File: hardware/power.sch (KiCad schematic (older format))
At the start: 18 parts

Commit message: przeniosiono do folderu hardware
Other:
- note added: "analog & digital voltage split\n"
- note removed: "voltage analog & digital voltage split\n"
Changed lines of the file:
@@
 U 1 1 5D6AB170
 P 7400 3850
+AR Path="/5CDEAB6D/5D6AB170" Ref="FB?"  Part="1"
+AR Path="/5CDEEC5A/5D6AB170" Ref="FB?"  Part="1"
 F 0 "FB?" H 7500 3896 50  0000 L CNN
 F 1 "Ferrite_Bead_Small" H 7500 3805 50  0000 L CNN
@@
 U 1 1 5D6AB176
 P 7650 3850
+AR Path="/5CDEAB6D/5D6AB176" Ref="#PWR?"  Part="1"
+AR Path="/5CDEEC5A/5D6AB176" Ref="#PWR?"  Part="1"
 F 0 "#PWR?" H 7650 3700 50  0001 C CNN
 F 1 "+3.3V" V 7665 3978 50  0000 L CNN
@@
 	6650 3400 6650 3700
 Text Notes 6650 3350 0    50   ~ 0
-voltage analog & digital voltage split\n
+analog & digital voltage split\n
 $EndSCHEMATC

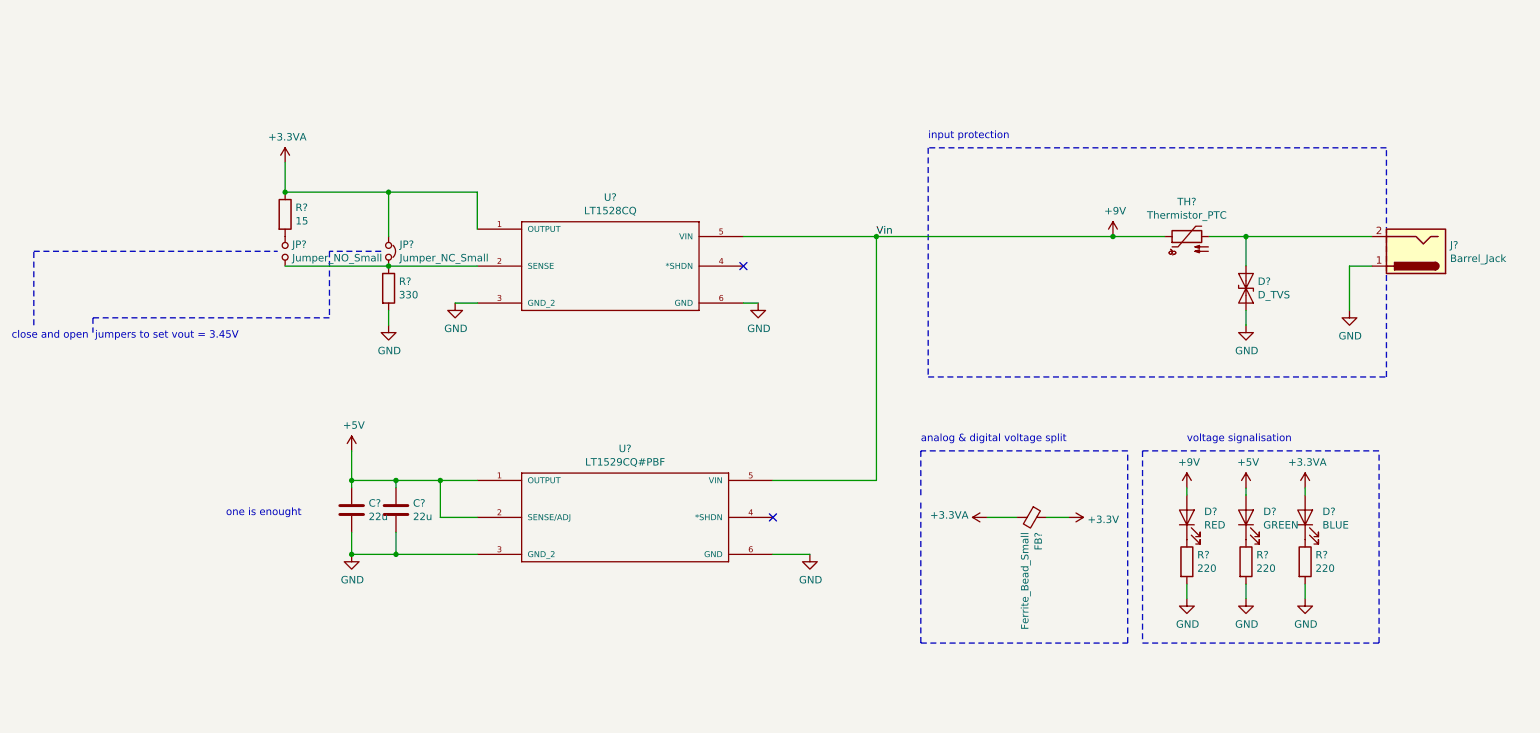
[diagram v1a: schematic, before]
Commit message: DRC przechodzi dorzucone złącze do wyświetlacza na i2c oraz jeden push button
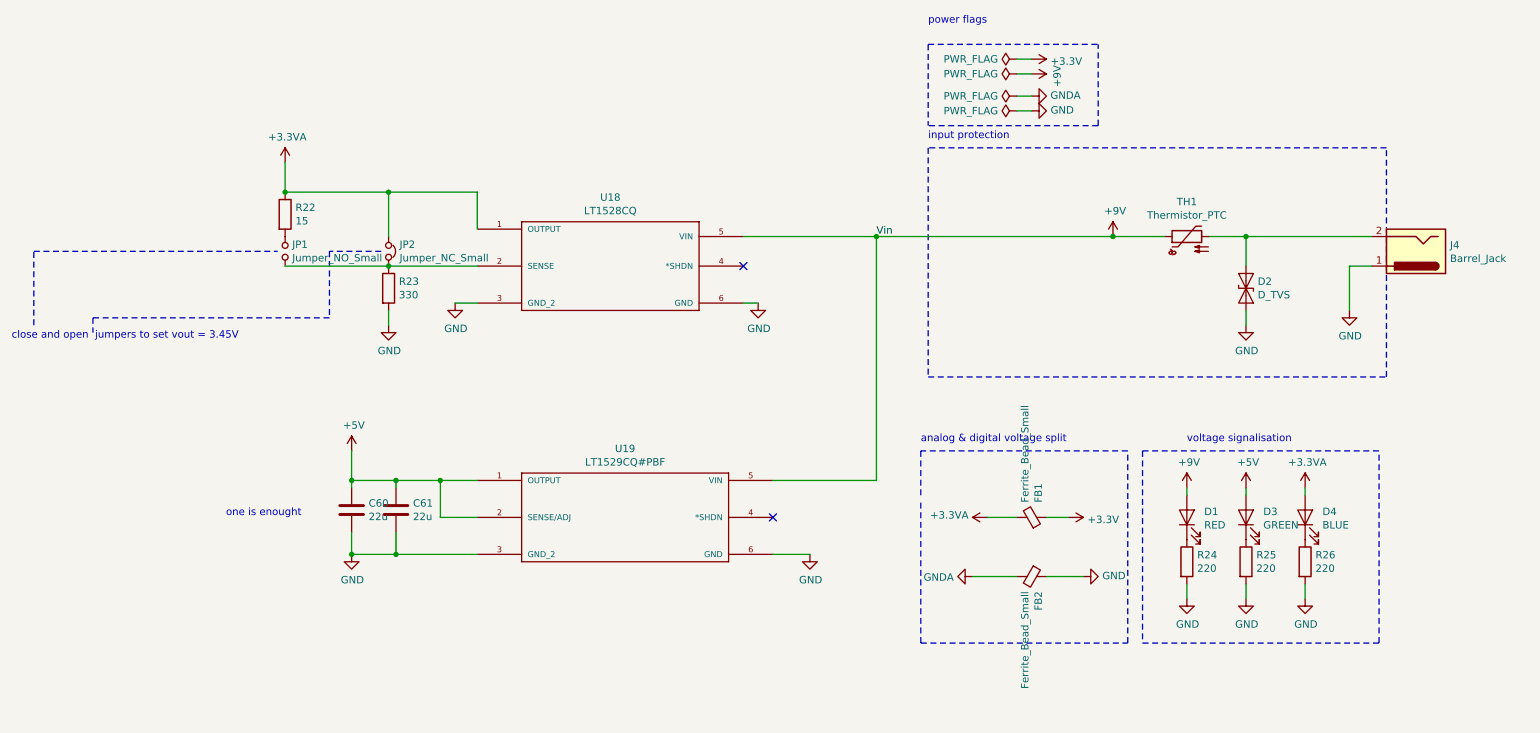
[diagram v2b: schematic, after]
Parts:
- added FB2: Ferrite_Bead_Small, symbol Device:Ferrite_Bead_Small
- gave numbers to parts that had none: 18
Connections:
- net GND: now also FB2.1
- new net GNDA: FB2.2
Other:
- note added: "power flags\n\n"

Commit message: przypisano footprinty
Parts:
- C60, C61: footprint (none) -> Capacitor_SMD:C_0805_2012Metric_Pad1.15x1.40mm_HandSolder
- D1, D3, D4: footprint (none) -> LED_SMD:LED_0805_2012Metric
- D2: footprint (none) -> Diode_SMD:D_SOD-323
- FB1, FB2: footprint (none) -> Inductor_SMD:L_0805_2012Metric_Pad1.15x1.40mm_HandSolder
- J4: footprint (none) -> Connector_BarrelJack:BarrelJack_Horizontal
- JP1: footprint (none) -> Jumper:SolderJumper-2_P1.3mm_Open_TrianglePad1.0x1.5mm
- JP2: footprint (none) -> Jumper:SolderJumper-2_P1.3mm_Bridged_Pad1.0x1.5mm
- R22, R23, R24, R25, R26: footprint (none) -> Resistor_SMD:R_0603_1608Metric_Pad1.05x0.95mm_HandSolder
- TH1: footprint (none) -> Fuse:Fuse_1812_4532Metric
- U18, U19: footprint DDPAK-5_Q -> symbols:DDPAK-5_Q
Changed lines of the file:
@@
 $Descr A4 11693 8268
 encoding utf-8
-Sheet 5 4
+Sheet 4 4
 Title ""
 Date ""
@@
 F 0 "U18" H 4550 2415 50  0000 C CNN
 F 1 "LT1528CQ" H 4550 2324 50  0000 C CNN
-F 2 "DDPAK-5_Q" H 3650 2050 50  0001 L BNN
+F 2 "symbols:DDPAK-5_Q" H 3650 2050 50  0001 L BNN
 F 3 "" H 3650 2050 50  0001 L BNN
 F 4 "None" H 3650 2050 50  0001 L BNN "Pole4"
@@
 F 0 "U19" H 4650 4115 50  0000 C CNN
 F 1 "LT1529CQ#PBF" H 4650 4024 50  0000 C CNN
-F 2 "DDPAK-5_Q" H 3650 3750 50  0001 L BNN
+F 2 "symbols:DDPAK-5_Q" H 3650 3750 50  0001 L BNN
 F 3 "" H 3650 3750 50  0001 L BNN
 F 4 "TO-263 Linear Technology" H 3650 3750 50  0001 L BNN "Pole4"
@@
 F 0 "R23" H 3120 2346 50  0000 L CNN
 F 1 "330" H 3120 2255 50  0000 L CNN
-F 2 "" V 2980 2300 50  0001 C CNN
+F 2 "Resistor_SMD:R_0603_1608Metric_Pad1.05x0.95mm_HandSolder" V 2980 2300 50  0001 C CNN
 F 3 "~" H 3050 2300 50  0001 C CNN
 	1    3050 2300
@@
 F 0 "R22" H 2420 1846 50  0000 L CNN
 F 1 "15" H 2420 1755 50  0000 L CNN
-F 2 "" V 2280 1800 50  0001 C CNN
+F 2 "Resistor_SMD:R_0603_1608Metric_Pad1.05x0.95mm_HandSolder" V 2280 1800 50  0001 C CNN
 F 3 "~" H 2350 1800 50  0001 C CNN
 	1    2350 1800
@@
 F 0 "JP2" V 3004 2124 50  0000 L CNN
 F 1 "Jumper_NC_Small" V 3095 2124 50  0000 L CNN
-F 2 "" H 3050 2050 50  0001 C CNN
+F 2 "Jumper:SolderJumper-2_P1.3mm_Bridged_Pad1.0x1.5mm" H 3050 2050 50  0001 C CNN
 F 3 "~" H 3050 2050 50  0001 C CNN
 	1    3050 2050
@@
 F 0 "JP1" V 2396 2002 50  0000 R CNN
 F 1 "Jumper_NO_Small" V 2305 2002 50  0000 R CNN
-F 2 "" H 2350 2050 50  0001 C CNN
+F 2 "Jumper:SolderJumper-2_P1.3mm_Open_TrianglePad1.0x1.5mm" H 2350 2050 50  0001 C CNN
 F 3 "~" H 2350 2050 50  0001 C CNN
 	1    2350 2050
@@
 F 0 "C60" H 2915 3846 50  0000 L CNN
 F 1 "22u" H 2915 3755 50  0000 L CNN
-F 2 "" H 2838 3650 50  0001 C CNN
+F 2 "Capacitor_SMD:C_0805_2012Metric_Pad1.15x1.40mm_HandSolder" H 2838 3650 50  0001 C CNN
 F 3 "~" H 2800 3800 50  0001 C CNN
 	1    2800 3800
@@
 F 0 "C61" H 3215 3846 50  0000 L CNN
 F 1 "22u" H 3215 3755 50  0000 L CNN
-F 2 "" H 3138 3650 50  0001 C CNN
+F 2 "Capacitor_SMD:C_0805_2012Metric_Pad1.15x1.40mm_HandSolder" H 3138 3650 50  0001 C CNN
 F 3 "~" H 3100 3800 50  0001 C CNN
 	1    3100 3800
@@
 F 0 "J4" H 9770 2008 50  0000 R CNN
 F 1 "Barrel_Jack" H 9770 2099 50  0000 R CNN
-F 2 "" H 10050 2010 50  0001 C CNN
+F 2 "Connector_BarrelJack:BarrelJack_Horizontal" H 10050 2010 50  0001 C CNN
 F 3 "~" H 10050 2010 50  0001 C CNN
 	1    10000 2050
@@
 F 0 "D4" V 9289 3733 50  0000 R CNN
 F 1 "BLUE" V 9198 3733 50  0000 R CNN
-F 2 "" H 9250 3850 50  0001 C CNN
+F 2 "LED_SMD:LED_0805_2012Metric" H 9250 3850 50  0001 C CNN
 F 3 "~" H 9250 3850 50  0001 C CNN
 	1    9250 3850
@@
 F 0 "R26" H 9320 4196 50  0000 L CNN
 F 1 "220" H 9320 4105 50  0000 L CNN
-F 2 "" V 9180 4150 50  0001 C CNN
+F 2 "Resistor_SMD:R_0603_1608Metric_Pad1.05x0.95mm_HandSolder" V 9180 4150 50  0001 C CNN
 F 3 "~" H 9250 4150 50  0001 C CNN
 	1    9250 4150
@@
 F 0 "D3" V 8889 3733 50  0000 R CNN
 F 1 "GREEN" V 8798 3733 50  0000 R CNN
-F 2 "" H 8850 3850 50  0001 C CNN
+F 2 "LED_SMD:LED_0805_2012Metric" H 8850 3850 50  0001 C CNN
 F 3 "~" H 8850 3850 50  0001 C CNN
 	1    8850 3850
@@
 F 0 "R25" H 8920 4196 50  0000 L CNN
 F 1 "220" H 8920 4105 50  0000 L CNN
-F 2 "" V 8780 4150 50  0001 C CNN
+F 2 "Resistor_SMD:R_0603_1608Metric_Pad1.05x0.95mm_HandSolder" V 8780 4150 50  0001 C CNN
 F 3 "~" H 8850 4150 50  0001 C CNN
 	1    8850 4150
@@
 F 0 "D1" V 8489 3733 50  0000 R CNN
 F 1 "RED" V 8398 3733 50  0000 R CNN
-F 2 "" H 8450 3850 50  0001 C CNN
+F 2 "LED_SMD:LED_0805_2012Metric" H 8450 3850 50  0001 C CNN
 F 3 "~" H 8450 3850 50  0001 C CNN
 	1    8450 3850
@@
 F 0 "R24" H 8520 4196 50  0000 L CNN
 F 1 "220" H 8520 4105 50  0000 L CNN
-F 2 "" V 8380 4150 50  0001 C CNN
+F 2 "Resistor_SMD:R_0603_1608Metric_Pad1.05x0.95mm_HandSolder" V 8380 4150 50  0001 C CNN
 F 3 "~" H 8450 4150 50  0001 C CNN
 	1    8450 4150
@@
 F 0 "TH1" V 8685 1950 50  0000 C CNN
 F 1 "Thermistor_PTC" V 8594 1950 50  0000 C CNN
-F 2 "" H 8500 1750 50  0001 L CNN
+F 2 "Fuse:Fuse_1812_4532Metric" H 8500 1750 50  0001 L CNN
 F 3 "~" H 8450 1950 50  0001 C CNN
 	1    8450 1950
@@
 F 0 "D2" V 8804 2379 50  0000 L CNN
 F 1 "D_TVS" V 8895 2379 50  0000 L CNN
-F 2 "" H 8850 2300 50  0001 C CNN
+F 2 "Diode_SMD:D_SOD-323" H 8850 2300 50  0001 C CNN
 F 3 "~" H 8850 2300 50  0001 C CNN
 	1    8850 2300
@@
 F 0 "FB1" H 7500 3896 50  0000 L CNN
 F 1 "Ferrite_Bead_Small" H 7500 3805 50  0000 L CNN
-F 2 "" V 7330 3850 50  0001 C CNN
+F 2 "Inductor_SMD:L_0805_2012Metric_Pad1.15x1.40mm_HandSolder" V 7330 3850 50  0001 C CNN
 F 3 "~" H 7400 3850 50  0001 C CNN
 	1    7400 3850
@@
 F 0 "FB2" H 7500 4296 50  0000 L CNN
 F 1 "Ferrite_Bead_Small" H 7500 4205 50  0000 L CNN
-F 2 "" V 7330 4250 50  0001 C CNN
+F 2 "Inductor_SMD:L_0805_2012Metric_Pad1.15x1.40mm_HandSolder" V 7330 4250 50  0001 C CNN
 F 3 "~" H 7400 4250 50  0001 C CNN
 	1    7400 4250

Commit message: Dodenie pullup do spi i i2c
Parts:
- D2: footprint Diode_SMD:D_SOD-323 -> Diode_SMD:D_SMB
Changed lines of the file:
@@
 F 0 "D2" V 8804 2379 50  0000 L CNN
 F 1 "D_TVS" V 8895 2379 50  0000 L CNN
-F 2 "Diode_SMD:D_SOD-323" H 8850 2300 50  0001 C CNN
+F 2 "Diode_SMD:D_SMB" H 8850 2300 50  0001 C CNN
 F 3 "~" H 8850 2300 50  0001 C CNN
 	1    8850 2300

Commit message: pierwszy układ PCB
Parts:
- added C62, C63: 10u, Capacitor_SMD:C_0805_2012Metric_Pad1.15x1.40mm_HandSolder, symbol Device:C
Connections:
- net +5V: now also U18.5 (VIN), C63.1
- net +9V: now also C62.1; no longer U18.5 (VIN)
- net GND: now also C62.2, C63.2
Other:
- moved on the sheet: C60, C61, JP1, JP2, R22, R23, U18, U19

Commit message: update pinoutu, zmiany footprintów
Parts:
- removed JP1: Jumper_NO_Small, Jumper:SolderJumper-2_P1.3mm_Open_TrianglePad1.0x1.5mm, symbol Device:Jumper_NO_Small
- R22: value 15 -> N.C
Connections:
- net +9V: now also D2.1 (A1)
- net at JP2.2, R23.1, U18.2 (SENSE): now also R22.2
- net at J4.2, TH1.2: no longer D2.1 (A1)
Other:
- note added: "open jumper to set vout = 3.45V\nset R to 15"
- note removed: "close and open jumpers to set vout = 3.45V\n"
- moved on the sheet: D2
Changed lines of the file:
@@
 P 2650 4050
 F 0 "R22" H 2720 4096 50  0000 L CNN
-F 1 "15" H 2720 4005 50  0000 L CNN
+F 1 "N.C" H 2720 4005 50  0000 L CNN
 F 2 "Resistor_SMD:R_0603_1608Metric_Pad1.05x0.95mm_HandSolder" V 2580 4050 50  0001 C CNN
 F 3 "~" H 2650 4050 50  0001 C CNN
@@
 Wire Wire Line
 	5850 4650 5750 4650
-$Comp
-L Device:Jumper_NO_Small JP1
-U 1 1 5CEC3FA4
-P 2650 4300
-F 0 "JP1" V 2696 4252 50  0000 R CNN
-F 1 "Jumper_NO_Small" V 2605 4252 50  0000 R CNN
-F 2 "Jumper:SolderJumper-2_P1.3mm_Open_TrianglePad1.0x1.5mm" H 2650 4300 50  0001 C CNN
-F 3 "~" H 2650 4300 50  0001 C CNN
-	1    2650 4300
-	0    -1   -1   0
-$EndComp
 Wire Wire Line
 	2650 4400 3350 4400
@@
 	2650 3900 3350 3900
 Text Notes 800  4900 0    50   ~ 0
-close and open  jumpers to set vout = 3.45V\n
+open  jumper to set vout = 3.45V\nset R to 15
 Connection ~ 2650 3900
 NoConn ~ 5600 2200
@@
 Wire Wire Line
 	2750 2450 3050 2450
-Wire Notes Line
-	950  4800 950  4300
-Wire Notes Line
-	950  4300 2600 4300
 Wire Notes Line
 	3300 4300 2950 4300
@@
 $EndComp
 Wire Wire Line
-	8300 1950 7950 1950
+	8300 1950 8150 1950
 $Comp
 L Device:D_TVS D2
 U 1 1 5D3648D0
-P 8850 2300
-F 0 "D2" V 8804 2379 50  0000 L CNN
-F 1 "D_TVS" V 8895 2379 50  0000 L CNN
-F 2 "Diode_SMD:D_SMB" H 8850 2300 50  0001 C CNN
-F 3 "~" H 8850 2300 50  0001 C CNN
-	1    8850 2300
+P 8150 2300
+F 0 "D2" V 8104 2379 50  0000 L CNN
+F 1 "D_TVS" V 8195 2379 50  0000 L CNN
+F 2 "Diode_SMD:D_SMB" H 8150 2300 50  0001 C CNN
+F 3 "~" H 8150 2300 50  0001 C CNN
+	1    8150 2300
 	0    1    1    0
 $EndComp
 Wire Wire Line
-	8850 1950 8850 2150
-Connection ~ 8850 1950
-Wire Wire Line
-	8850 1950 8600 1950
+	8150 1950 8150 2150
 $Comp
 L power:GND #PWR0128
 U 1 1 5D365DC5
-P 8850 2550
-F 0 "#PWR0128" H 8850 2300 50  0001 C CNN
-F 1 "GND" H 8855 2377 50  0000 C CNN
-F 2 "" H 8850 2550 50  0001 C CNN
-F 3 "" H 8850 2550 50  0001 C CNN
-	1    8850 2550
-	1    0    0    -1
-$EndComp
-Wire Wire Line
-	8850 2450 8850 2550
-Wire Wire Line
-	8850 1950 9700 1950
+P 8150 2550
+F 0 "#PWR0128" H 8150 2300 50  0001 C CNN
+F 1 "GND" H 8155 2377 50  0000 C CNN
+F 2 "" H 8150 2550 50  0001 C CNN
+F 3 "" H 8150 2550 50  0001 C CNN
+	1    8150 2550
+	1    0    0    -1
+$EndComp
+Wire Wire Line
+	8150 2450 8150 2550
 $Comp
 L power:+3.3VA #PWR0116
@@
 	6050 2450 6050 2250
 Connection ~ 5850 2450
+Connection ~ 8150 1950
+Wire Wire Line
+	8150 1950 7950 1950
+Wire Wire Line
+	8600 1950 9700 1950
+Wire Wire Line
+	2650 4200 2650 4400
+Wire Notes Line
+	800  4850 650  4850
+Wire Notes Line
+	650  4050 650  4850
+Wire Notes Line
+	650  4050 2550 4050
 $EndSCHEMATC

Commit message: dodanie zabezpieczen portów i dzialniki napiec na wejsciach adc
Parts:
- renumbered C60 to C62, C61 to C63, C62 to C64, C63 to C65, D1 to D3, D3 to D4, D4 to D5, J4 to J7, JP2 to JP1, R22 to R50, R23 to R51, R24 to R52, R25 to R53, R26 to R54, U19 to U18, U18 to U19

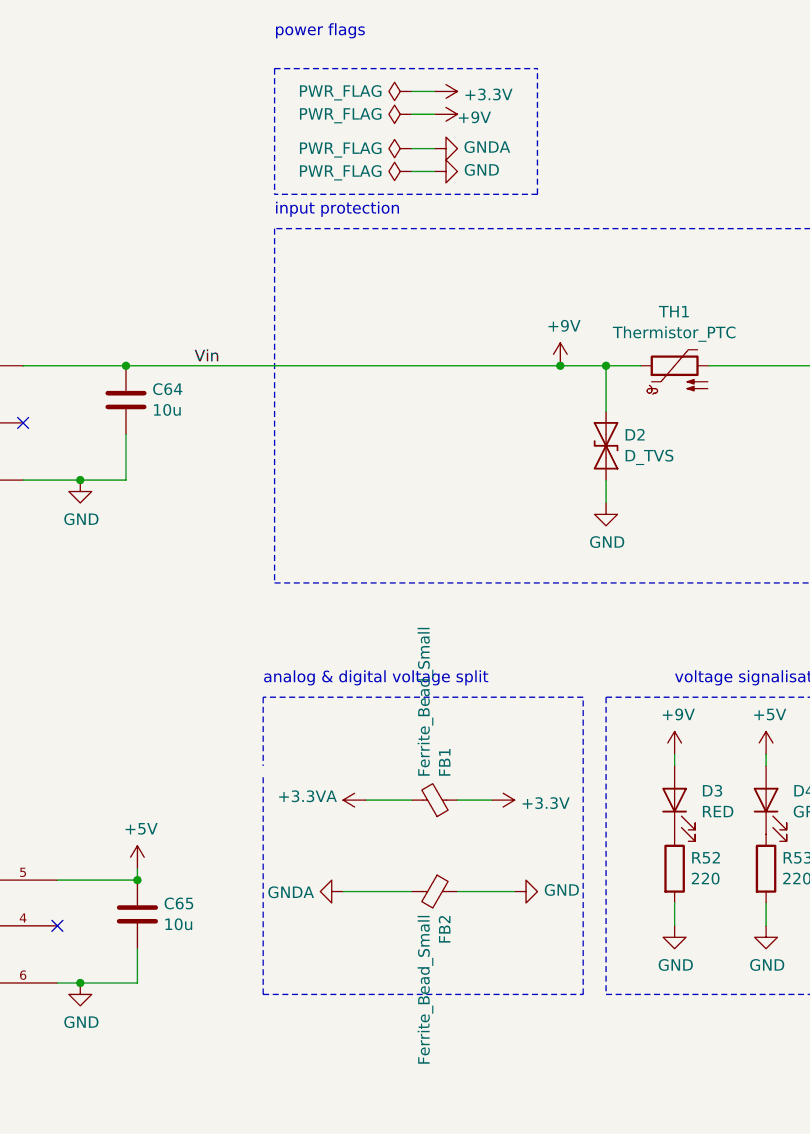
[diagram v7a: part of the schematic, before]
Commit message: layout gotów, do wyeliminowania błedy DRC
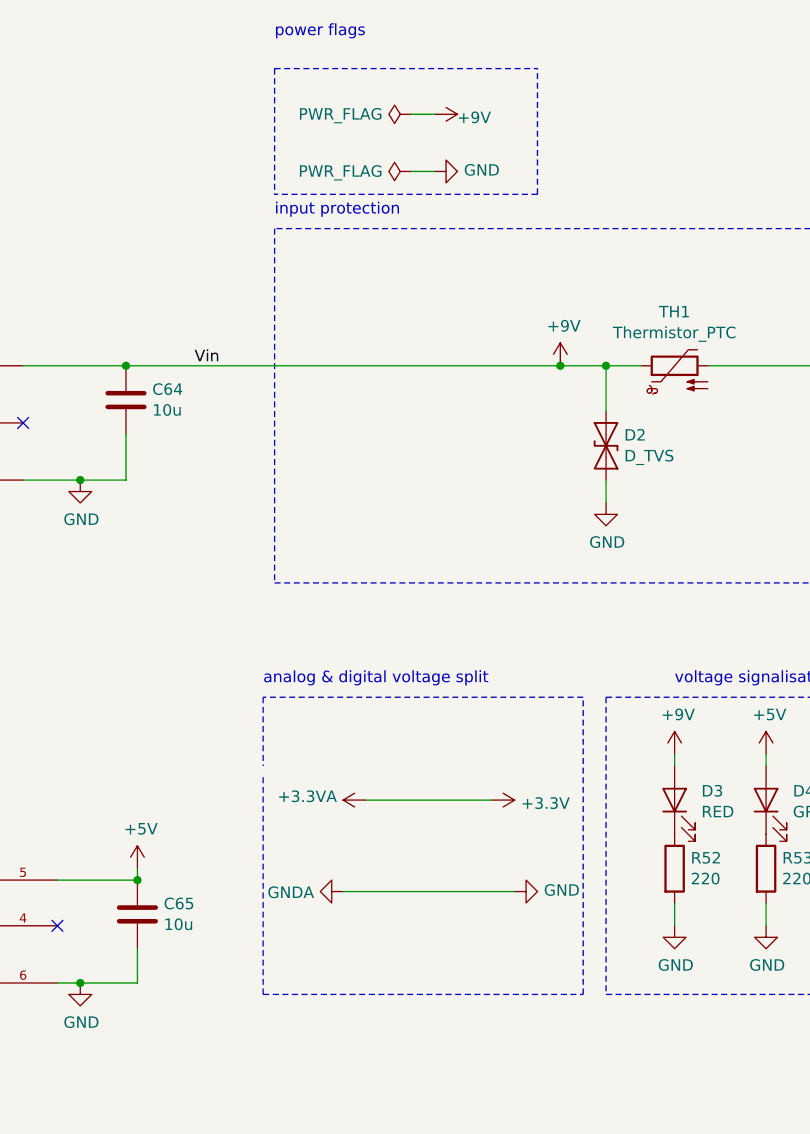
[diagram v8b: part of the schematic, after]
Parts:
- removed FB1, FB2: Ferrite_Bead_Small, Inductor_SMD:L_0805_2012Metric_Pad1.15x1.40mm_HandSolder, symbol Device:Ferrite_Bead_Small
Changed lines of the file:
@@
-$EndComp
-$Comp
-L Device:Ferrite_Bead_Small FB?
-U 1 1 5D6AB170
-P 7400 3850
-AR Path="/5CDEAB6D/5D6AB170" Ref="FB?"  Part="1"
-AR Path="/5CDEEC5A/5D6AB170" Ref="FB1"  Part="1"
-F 0 "FB1" H 7500 3896 50  0000 L CNN
-F 1 "Ferrite_Bead_Small" H 7500 3805 50  0000 L CNN
-F 2 "Inductor_SMD:L_0805_2012Metric_Pad1.15x1.40mm_HandSolder" V 7330 3850 50  0001 C CNN
-F 3 "~" H 7400 3850 50  0001 C CNN
-	1    7400 3850
-	0    1    -1   0
 $EndComp
 $Comp
@@
 	0    1    1    0
 $EndComp
-Wire Wire Line
-	7650 3850 7500 3850
 $Comp
 L power:+3.3VA #PWR0146
@@
 	0    -1   -1   0
 $EndComp
-Wire Wire Line
-	7100 3850 7300 3850
 Wire Notes Line
 	6650 3750 6650 4700
@@
 Text Notes 6650 3350 0    50   ~ 0
 analog & digital voltage split\n
-$Comp
-L power:PWR_FLAG #FLG01
-U 1 1 5D20679D
-P 7300 750
-F 0 "#FLG01" H 7300 825 50  0001 C CNN
-F 1 "PWR_FLAG" V 7300 877 50  0000 L CNN
-F 2 "" H 7300 750 50  0001 C CNN
-F 3 "~" H 7300 750 50  0001 C CNN
-	1    7300 750
-	0    -1   -1   0
-$EndComp
 $Comp
 L power:GNDA #PWR?
@@
 	0    -1   -1   0
 $EndComp
-$Comp
-L Device:Ferrite_Bead_Small FB?
-U 1 1 5D2119F7
-P 7400 4250
-AR Path="/5CDEAB6D/5D2119F7" Ref="FB?"  Part="1"
-AR Path="/5CDEEC5A/5D2119F7" Ref="FB2"  Part="1"
-F 0 "FB2" H 7500 4296 50  0000 L CNN
-F 1 "Ferrite_Bead_Small" H 7500 4205 50  0000 L CNN
-F 2 "Inductor_SMD:L_0805_2012Metric_Pad1.15x1.40mm_HandSolder" V 7330 4250 50  0001 C CNN
-F 3 "~" H 7400 4250 50  0001 C CNN
-	1    7400 4250
-	0    1    1    0
-$EndComp
-Wire Wire Line
-	7750 4250 7500 4250
-Wire Wire Line
-	7300 4250 7000 4250
 Text Notes 6700 600  0    50   ~ 0
 power flags\n\n
@@
 $EndComp
 $Comp
-L power:PWR_FLAG #FLG03
-U 1 1 5D21BB43
-P 7300 1000
-F 0 "#FLG03" H 7300 1075 50  0001 C CNN
-F 1 "PWR_FLAG" V 7300 1127 50  0000 L CNN
-F 2 "" H 7300 1000 50  0001 C CNN
-F 3 "~" H 7300 1000 50  0001 C CNN
-	1    7300 1000
-	0    -1   -1   0
-$EndComp
-$Comp
 L power:GND #PWR?
 U 1 1 5D21C471
@@
 	1    7400 1100
 	0    -1   -1   0
-$EndComp
-$Comp
-L power:GNDA #PWR?
-U 1 1 5D21C8EE
-P 7400 1000
-AR Path="/5CDEAB6D/5D21C8EE" Ref="#PWR?"  Part="1"
-AR Path="/5CDEEC5A/5D21C8EE" Ref="#PWR0149"  Part="1"
-F 0 "#PWR0149" H 7400 750 50  0001 C CNN
-F 1 "GNDA" V 7405 873 50  0000 R CNN
-F 2 "" H 7400 1000 50  0001 C CNN
-F 3 "" H 7400 1000 50  0001 C CNN
-	1    7400 1000
-	0    -1   -1   0
-$EndComp
-$Comp
-L power:+3.3V #PWR?
-U 1 1 5D21CE94
-P 7400 750
-AR Path="/5CDEAB6D/5D21CE94" Ref="#PWR?"  Part="1"
-AR Path="/5CDEEC5A/5D21CE94" Ref="#PWR0147"  Part="1"
-F 0 "#PWR0147" H 7400 600 50  0001 C CNN
-F 1 "+3.3V" V 7415 878 50  0000 L CNN
-F 2 "" H 7400 750 50  0001 C CNN
-F 3 "" H 7400 750 50  0001 C CNN
-	1    7400 750
-	0    1    1    0
 $EndComp
 $Comp
@@
 Wire Wire Line
 	7300 850  7400 850
-Wire Wire Line
-	7300 750  7400 750
-Wire Wire Line
-	7300 1000 7400 1000
 Wire Wire Line
 	7400 1100 7300 1100
@@
 Wire Notes Line
 	650  4050 2550 4050
+Wire Wire Line
+	7100 3850 7650 3850
+Wire Wire Line
+	7000 4250 7750 4250
 $EndSCHEMATC
